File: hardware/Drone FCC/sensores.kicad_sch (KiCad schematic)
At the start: 16 parts

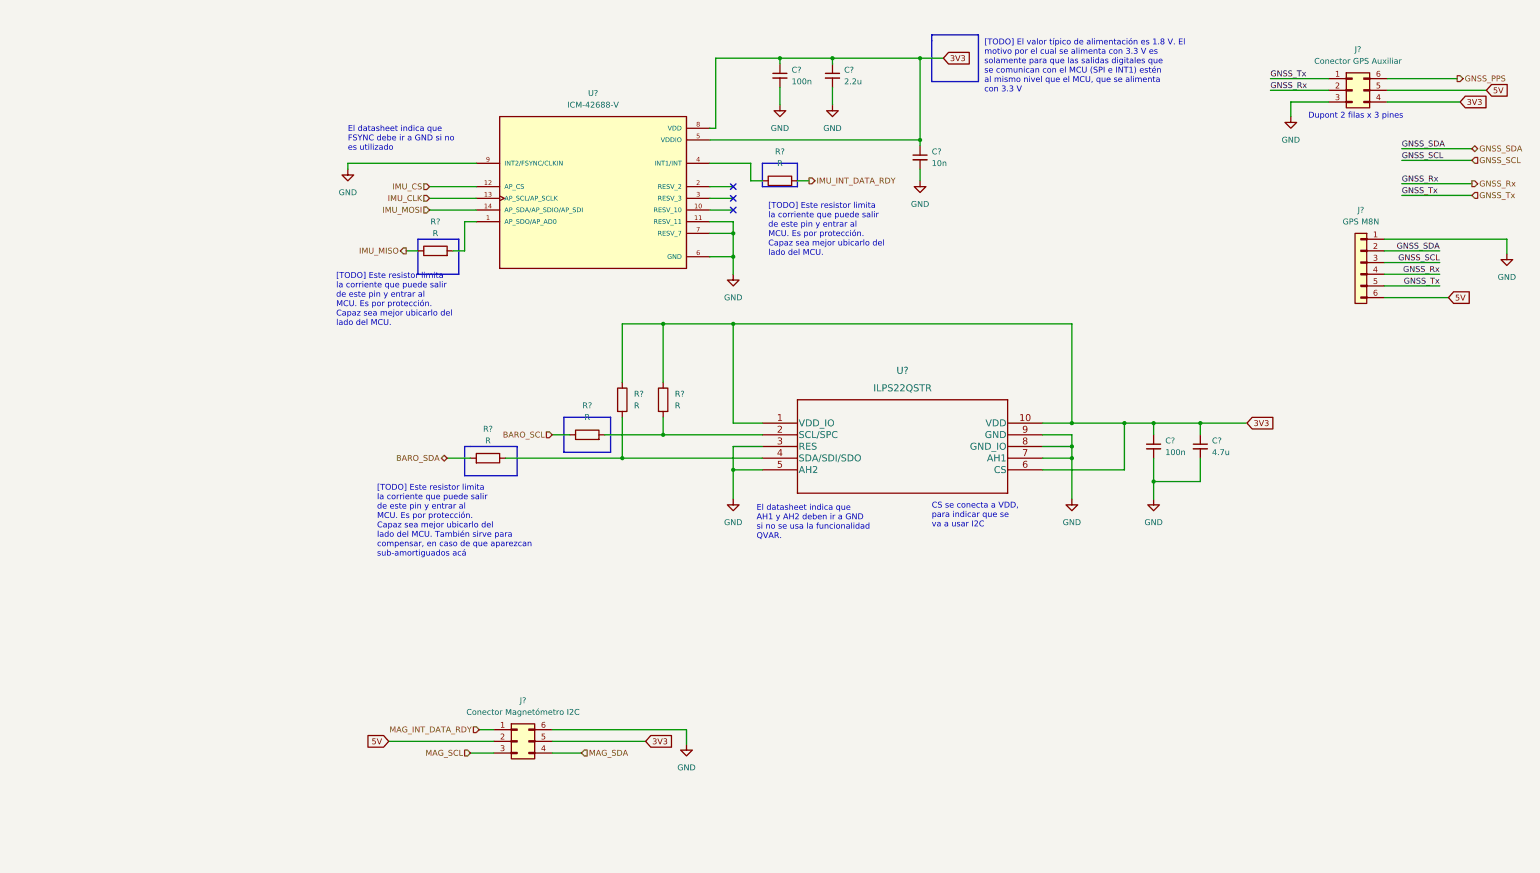
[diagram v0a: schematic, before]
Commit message: add USB connector
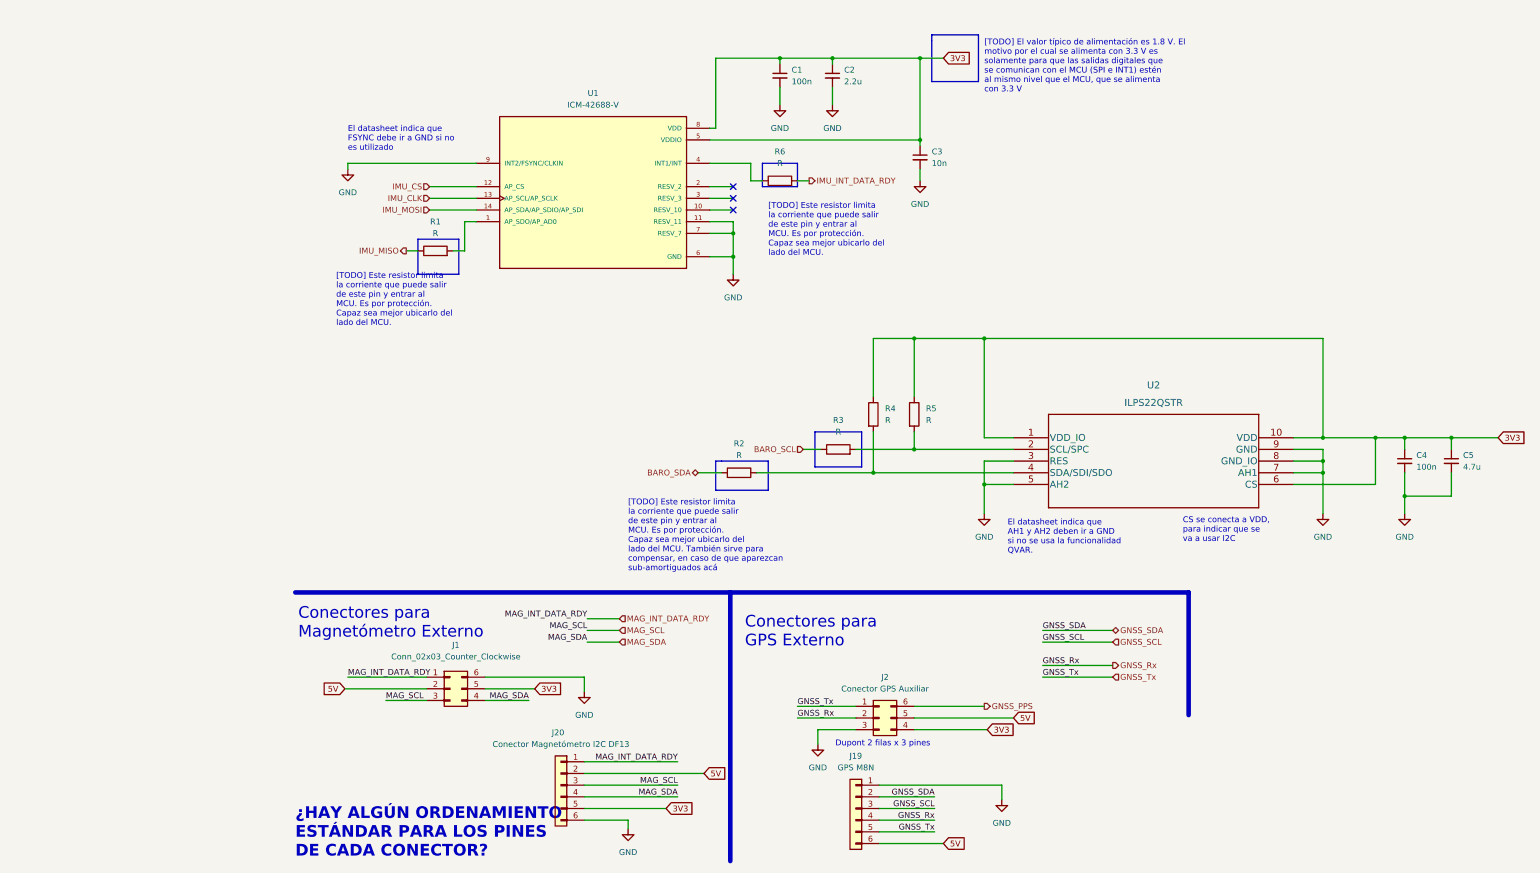
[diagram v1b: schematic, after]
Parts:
- removed J?: Conector Magnetómetro I2C, TSW-103-08-G-D-RA:SAMTEC_TSW-103-08-G-D-RA, symbol Connector_Generic:Conn_02x03_Counter_Clockwise
- added J1: Conn_02x03_Counter_Clockwise, TSW-103-08-G-D-RA:SAMTEC_TSW-103-08-G-D-RA, symbol Connector_Generic:Conn_02x03_Counter_Clockwise
- added J20: Conector Magnetómetro I2C DF13, Connector_Hirose:Hirose_DF13C_CL535-0406-3-51_1x06-1MP_P1.25mm_Vertical, symbol Connector_Generic:Conn_01x06
- gave numbers to parts that had none: 15
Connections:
- net 3V3: now also J1.5 (Pin_5), J20.5 (Pin_5)
- net 5V: now also J1.2 (Pin_2), J20.2 (Pin_2)
- net GND: now also J1.6 (Pin_6), J20.6 (Pin_6)
- net MAG_INT_DATA_RDY: now also J1.1 (Pin_1), J20.1 (Pin_1)
- net MAG_SCL: now also J1.3 (Pin_3), J20.3 (Pin_3)
- net MAG_SDA: now also J1.4 (Pin_4), J20.4 (Pin_4)
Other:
- note added: "Conectores para GPS Externo"
- note added: "Conectores para Magnetómetro Externo"
- note added: "¿HAY ALGÚN ORDENAMIENTO ESTÁNDAR PARA LOS PINES DE CADA CONECTOR?"
- moved on the sheet: C4, C5, J19, J2, R2, R3, R4, R5, U2

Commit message: DSM: deleted dupont conn, PPM: deleted DF-13 conn
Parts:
- J1, J2: footprint TSW-103-08-G-D-RA:SAMTEC_TSW-103-08-G-D-RA -> Connector_PinHeader_2.54mm:PinHeader_2x03_P2.54mm_Horizontal
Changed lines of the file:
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@@
     (property "Reference" "J2" (id 0) (at 141.605 156.845 0))
     (property "Value" "Conector GPS Auxiliar" (id 1) (at 141.605 159.385 0))
-    (property "Footprint" "TSW-103-08-G-D-RA:SAMTEC_TSW-103-08-G-D-RA" (id 2) (at 140.335 165.735 0)
+    (property "Footprint" "Connector_PinHeader_2.54mm:PinHeader_2x03_P2.54mm_Horizontal" (id 2) (at 140.335 165.735 0)
       (effects (font (size 1.27 1.27)) hide)
     )
@@
     (property "Reference" "J1" (id 0) (at 48.26 149.86 0))
     (property "Value" "Conn_02x03_Counter_Clockwise" (id 1) (at 48.26 152.4 0))
-    (property "Footprint" "TSW-103-08-G-D-RA:SAMTEC_TSW-103-08-G-D-RA" (id 2) (at 46.99 159.385 0)
+    (property "Footprint" "Connector_PinHeader_2.54mm:PinHeader_2x03_P2.54mm_Horizontal" (id 2) (at 46.99 159.385 0)
       (effects (font (size 1.27 1.27)) hide)
     )

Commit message: finished IMU basic schematic
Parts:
- removed R1, R6: R, symbol Device:R
- C1: value 100n -> 0.1u
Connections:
- net IMU_INT_DATA_RDY: now also U1.4 (INT1/INT)
- net IMU_MISO: now also U1.1 (AP_SDO/AP_AD0)
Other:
- note added: "IMU"
- note removed: "[TODO] El valor típico de alimentación es 1.8 V. El motivo por el cual se alimenta con 3.3 V es solamente para que las salidas digitales que se comunican con el MCU (SPI e INT1) estén al mismo nivel que el MCU, que se alimenta con 3.3 V"
- note removed: "[TODO] Este resistor limita la corriente que puede salir de este pin y entrar al MCU. Es por protección. Capaz sea mejor ubicarlo del lado del MCU."
- moved on the sheet: C1, C2, C3, U1

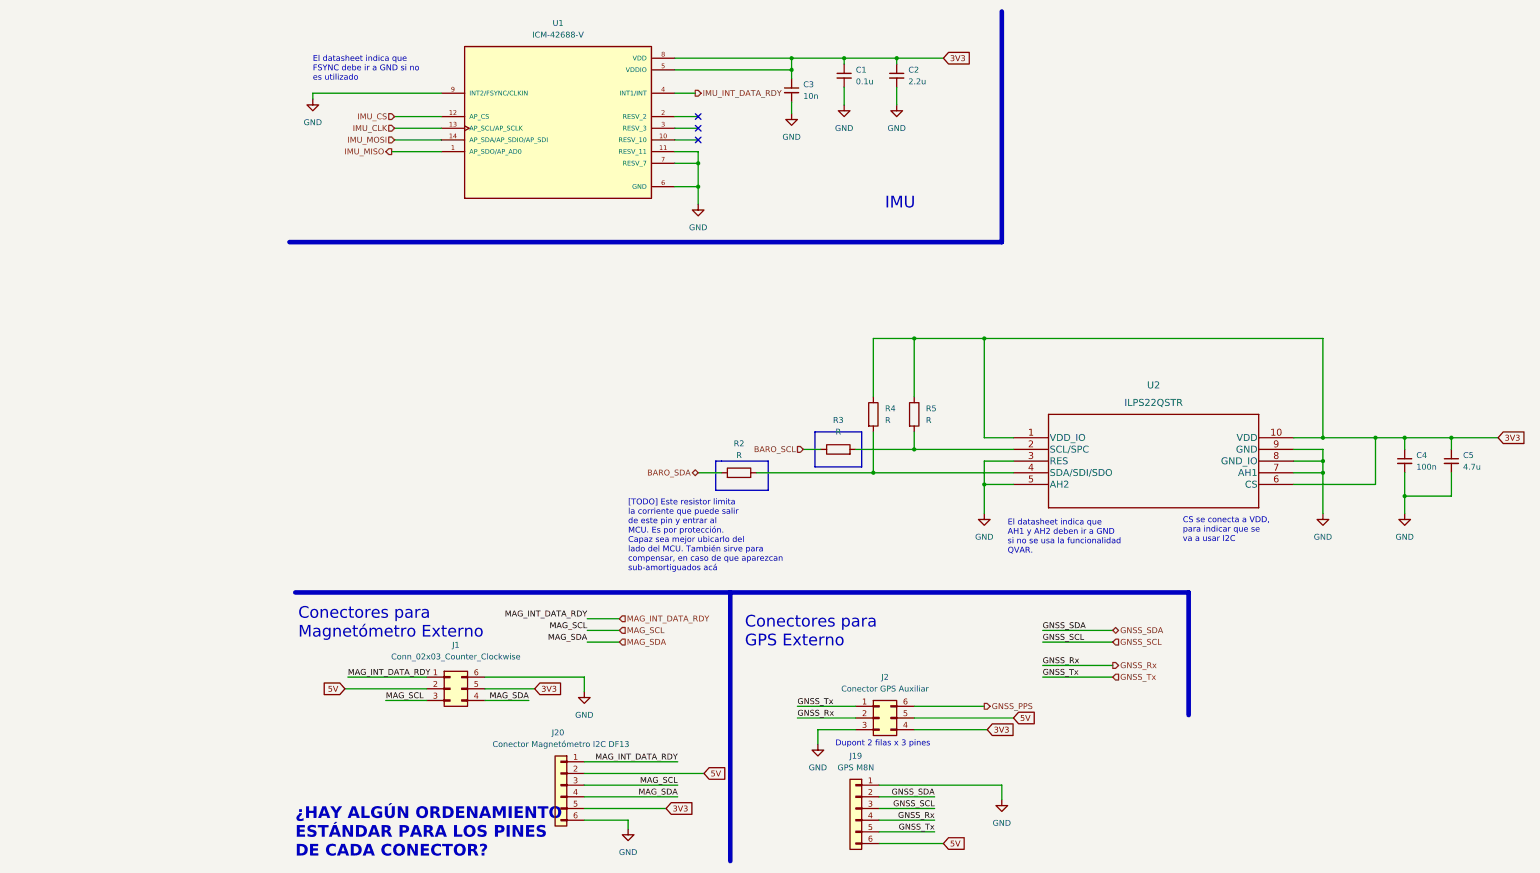
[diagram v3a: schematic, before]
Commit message: finish barometer schematic
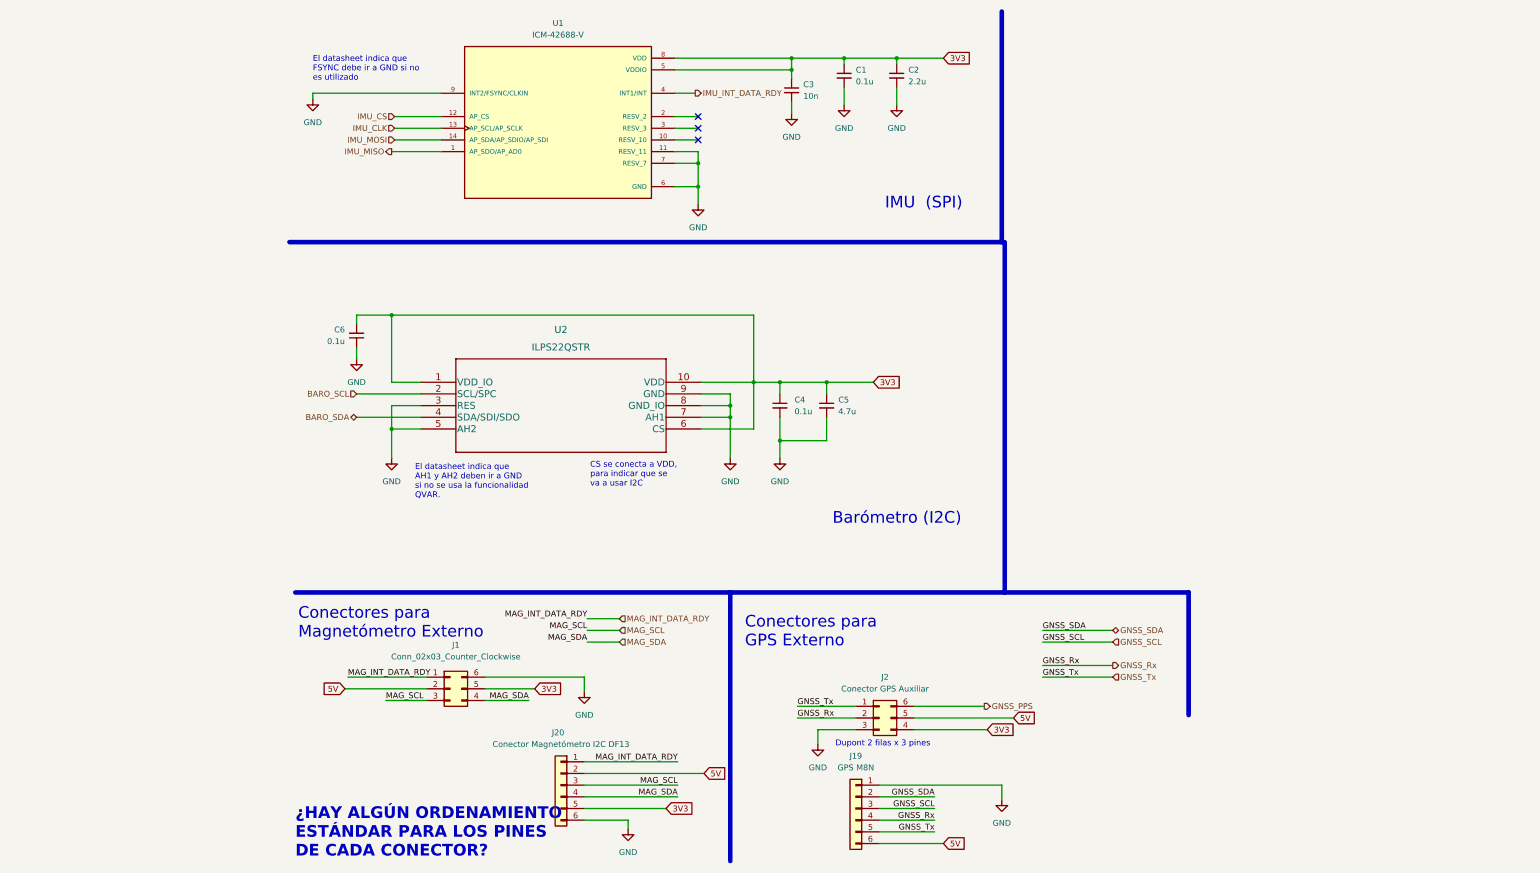
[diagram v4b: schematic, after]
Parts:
- removed R2, R3, R4, R5: R, symbol Device:R
- added C6: 0.1u, symbol Device:C_Small
- C4: value 100n -> 0.1u
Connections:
- net 3V3: now also C6.2
- net BARO_SCL: now also U2.2 (SCL/SPC)
- net BARO_SDA: now also U2.4 (SDA/SDI/SDO)
- net GND: now also C6.1
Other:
- note added: "Barómetro (I2C)"
- note added: "IMU (SPI)"
- note removed: "IMU"
- note removed: "[TODO] Este resistor limita la corriente que puede salir de este pin y entrar al MCU. Es por protección. Capaz sea mejor ubicarlo del lado del MCU. También sirve para compensar, en caso de que aparezcan sub-amortiguados acá"
- moved on the sheet: C4, C5, U2

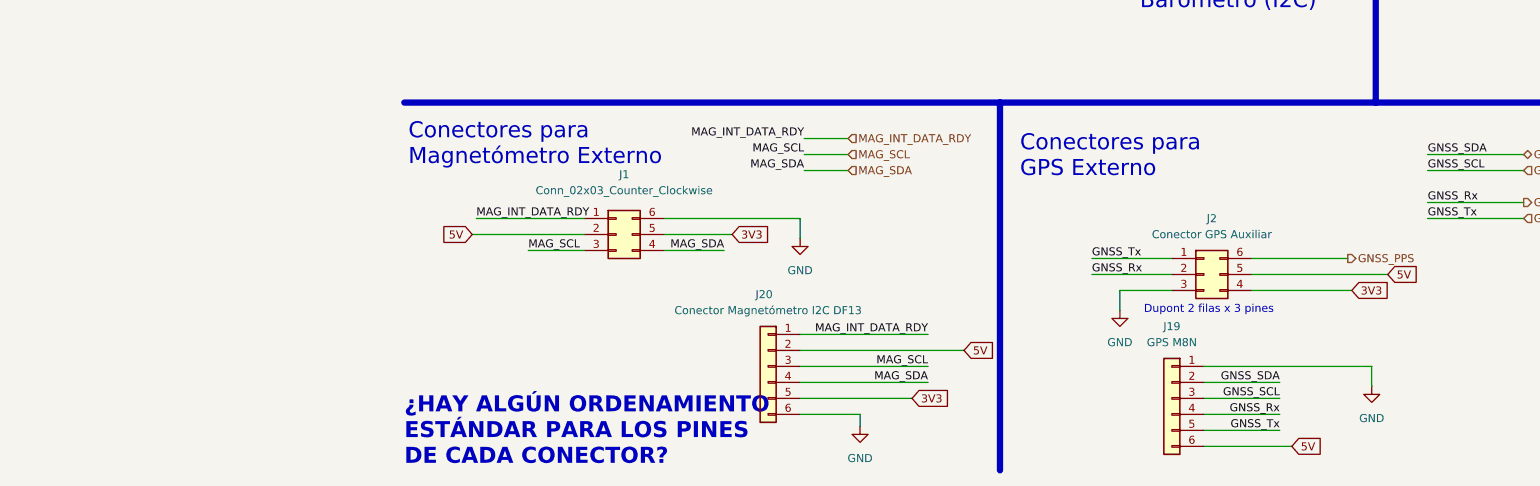
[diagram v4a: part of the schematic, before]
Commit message: moved MCU to hierarchical sheet
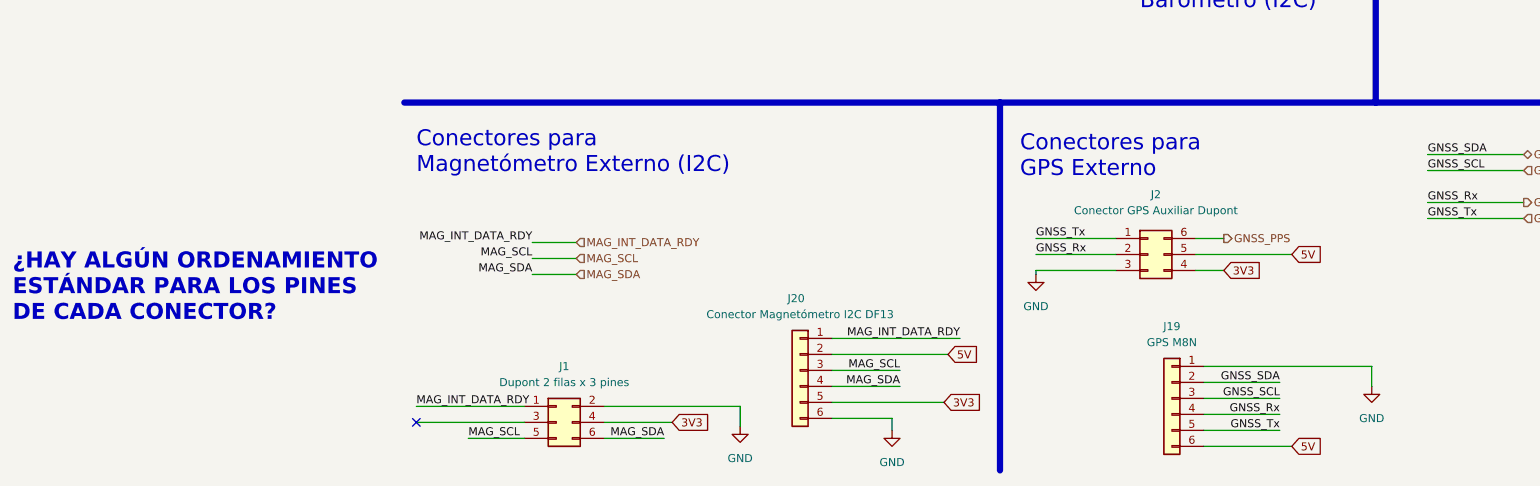
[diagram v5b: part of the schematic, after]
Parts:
- removed J1: Conn_02x03_Counter_Clockwise, Connector_PinHeader_2.54mm:PinHeader_2x03_P2.54mm_Horizontal, symbol Connector_Generic:Conn_02x03_Counter_Clockwise
- added J1: Dupont 2 filas x 3 pines, Connector_PinHeader_2.54mm:PinHeader_2x03_P2.54mm_Horizontal, symbol Connector_Generic:Conn_02x03_Odd_Even
- J2: value Conector GPS Auxiliar -> Conector GPS Auxiliar Dupont
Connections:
- net 3V3: now also J1.4 (Pin_4)
- net GND: now also J1.2 (Pin_2)
- net MAG_INT_DATA_RDY: now also J1.1 (Pin_1)
- net MAG_SCL: now also J1.5 (Pin_5)
- net MAG_SDA: now also J1.6 (Pin_6)
- no-connect marks 3 -> 4
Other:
- note added: "Conectores para Magnetómetro Externo (I2C)"
- note removed: "Conectores para Magnetómetro Externo"
- note removed: "Dupont 2 filas x 3 pines"
- moved on the sheet: J2, J20

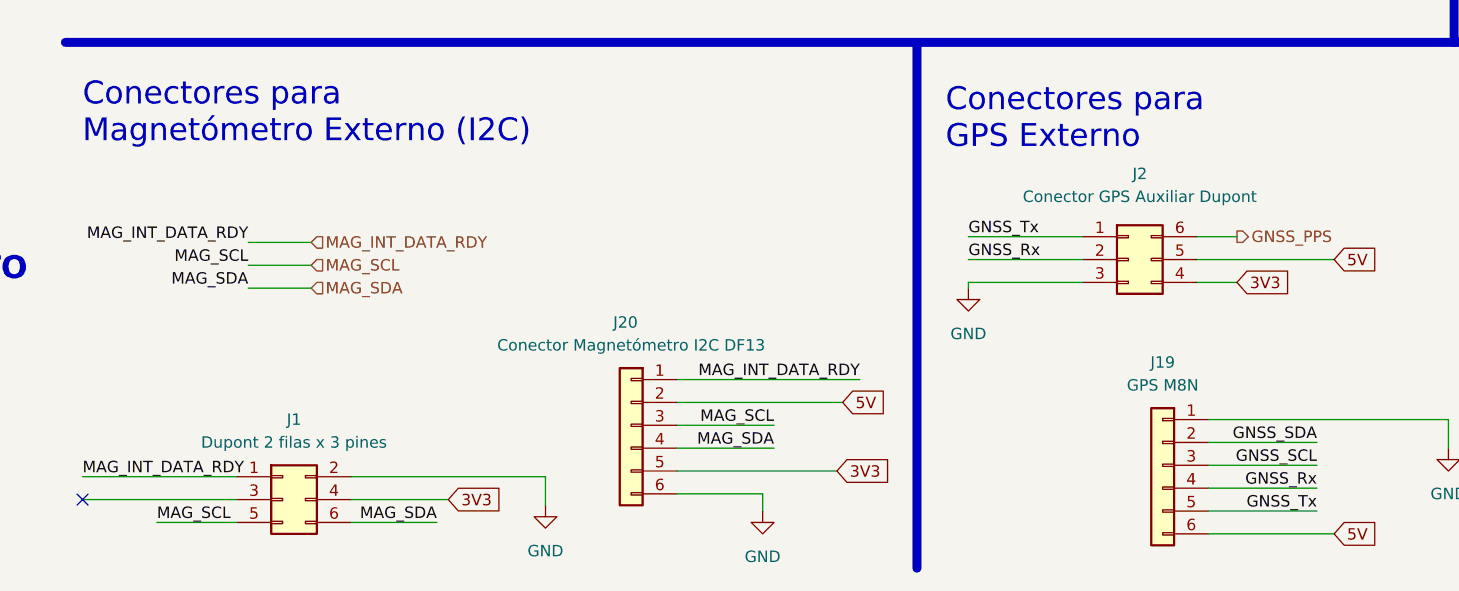
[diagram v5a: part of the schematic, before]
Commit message: changed mag connector for GPS module DF-13
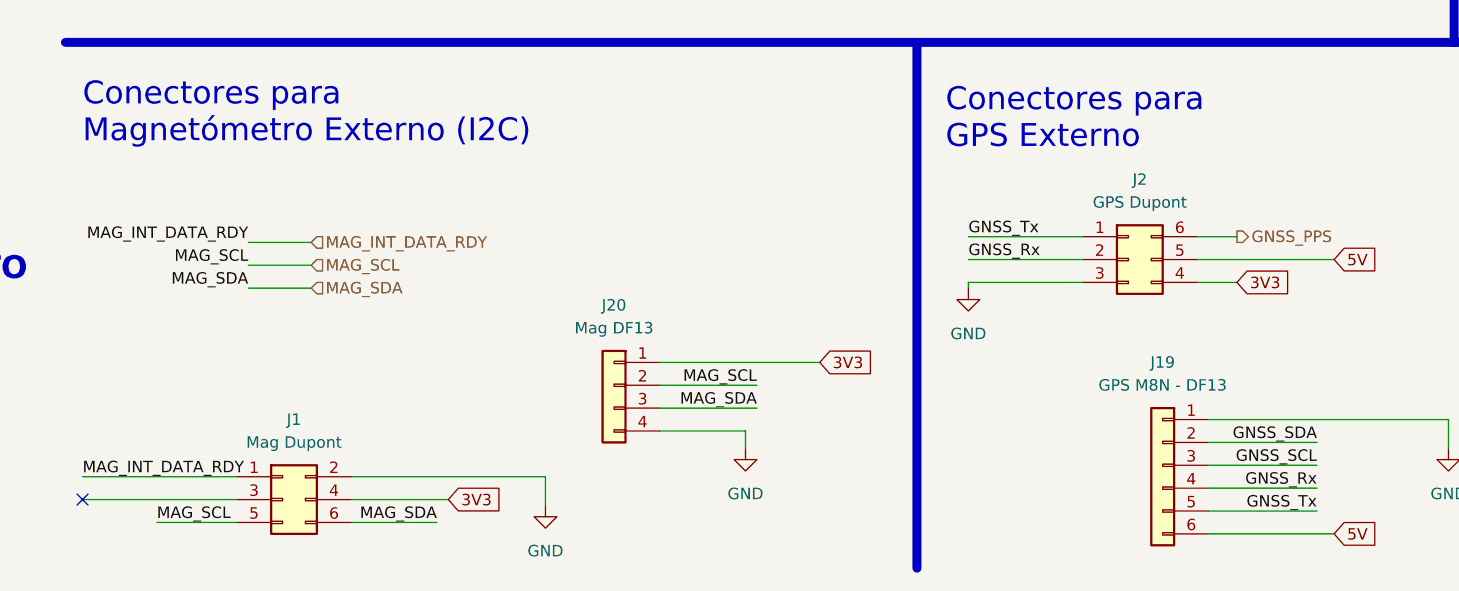
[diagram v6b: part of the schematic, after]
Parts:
- removed J20: Conector Magnetómetro I2C DF13, Connector_Hirose:Hirose_DF13C_CL535-0406-3-51_1x06-1MP_P1.25mm_Vertical, symbol Connector_Generic:Conn_01x06
- added J20: Mag DF13, Connector_Hirose:Hirose_DF13C_CL535-0404-8-51_1x04-1MP_P1.25mm_Vertical, symbol Connector_Generic:Conn_01x04
- J1: value Dupont 2 filas x 3 pines -> Mag Dupont
- J19: value GPS M8N -> GPS M8N - DF13
- J2: value Conector GPS Auxiliar Dupont -> GPS Dupont
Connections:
- net 3V3: now also J20.1 (Pin_1)
- net GND: now also J20.4 (Pin_4)
- net MAG_SCL: now also J20.2 (Pin_2)
- net MAG_SDA: now also J20.3 (Pin_3)
